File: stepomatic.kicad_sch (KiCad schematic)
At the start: 31 parts, among them J1 I2C, J2 28BYJ-48, J4 USB_B_Micro, Q1 MMBT3904, Q2 MMBT3904, SW1 Mode, SW2 RST, U1 HDC1080DMBR, U2 AMS1117-3.3, U3 ULN2003A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

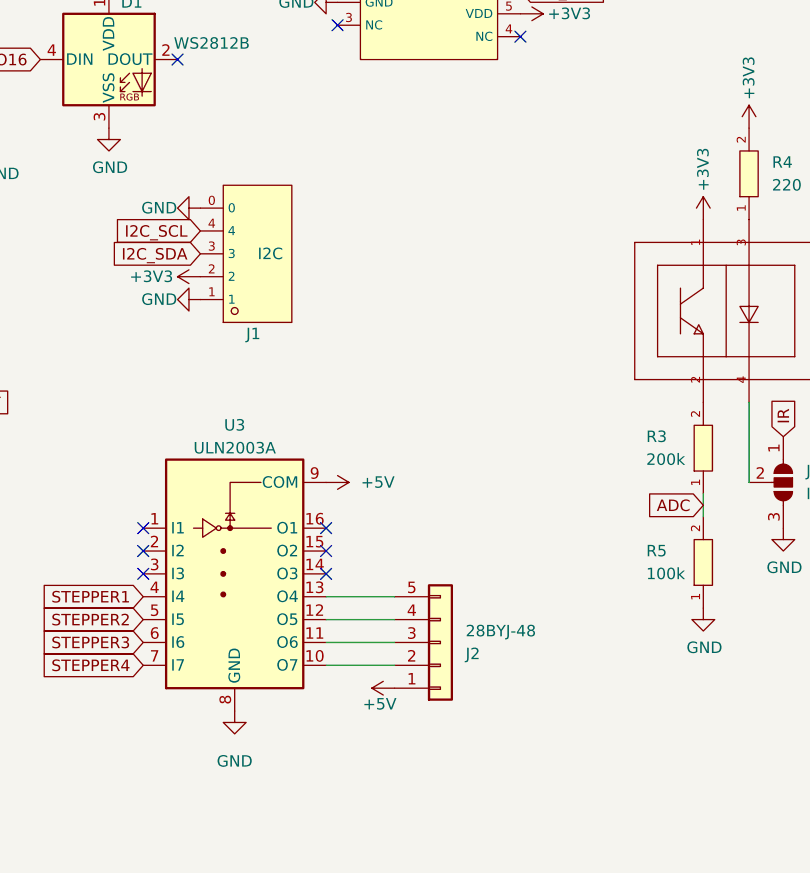
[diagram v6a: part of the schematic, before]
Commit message: Fix orientation of the stepper motor plug
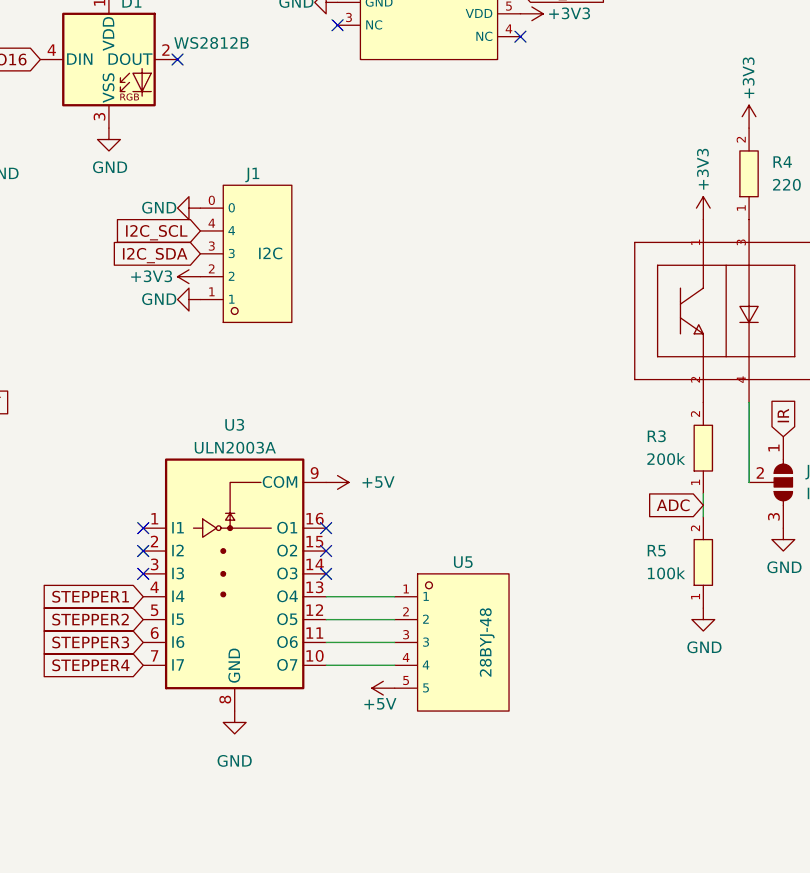
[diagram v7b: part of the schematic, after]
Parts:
- removed J2: 28BYJ-48, footprint:CONN-TH_B5B-XH-A-LF-SN, symbol Connector_Generic:Conn_01x05
- added U5: 28BYJ-48, footprint:CONN-TH_B5B-XH-A-LF-SN, symbol B5B-XH-A_(LF)(SN):B5B-XH-A_(LF)(SN)
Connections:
- net +5V: now also U5.5
- net at U3.10 (O7): now also U5.4
- net at U3.11 (O6): now also U5.3
- net at U3.12 (O5): now also U5.2
- net at U3.13 (O4): now also U5.1
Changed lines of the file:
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@@
   (symbol (lib_id "BM04B-SRSS-TB(LF)(SN):BM04B-SRSS-TB(LF)(SN)") (at 201.93 91.44 0) (mirror x) (unit 1)
     (in_bom yes) (on_board yes)
-    (property "Reference" "J1" (id 0) (at 201.93 100.33 0)
+    (property "Reference" "J1" (id 0) (at 201.93 82.55 0)
       (effects (font (size 1.27 1.27)) (justify left))
     )
@@
     )
     (pin "1")
+  )
+  (symbol (lib_id "B5B-XH-A_(LF)(SN):B5B-XH-A_(LF)(SN)") (at 224.79 134.62 0) (unit 1)
+    (in_bom yes) (on_board yes)
+    (property "Reference" "U5" (id 0) (at 226.06 125.73 0))
+    (property "Value" "28BYJ-48" (id 1) (at 228.6 134.62 90))
+    (property "Footprint" "footprint:CONN-TH_B5B-XH-A-LF-SN" (id 2) (at 224.79 144.78 0)
+      (effects (font (size 1.27 1.27) italic) hide)
+    )
+    (property "Datasheet" "https://atta.szlcsc.com/upload/public/pdf/source/20180319/EA947BC272645EB2E2B2116BA052A949.pdf" (id 3) (at 222.504 134.493 0)
+      (effects (font (size 1.27 1.27)) (justify left) hide)
+    )
+    (property "LCSC" "C157991" (id 4) (at 224.79 134.62 0)
+      (effects (font (size 1.27 1.27)) hide)
+    )
+    (pin "1")
+    (pin "2")
+    (pin "3")
+    (pin "4")
+    (pin "5")
   )
   (symbol (lib_id "power:+3V3") (at 186.69 62.23 0) (mirror y) (unit 1)
@@
     (pin "1")
   )
-  (symbol (lib_id "Connector_Generic:Conn_01x05") (at 223.52 134.62 0) (mirror x) (unit 1)
-    (in_bom yes) (on_board yes) (fields_autoplaced)
-    (property "Reference" "J2" (id 0) (at 226.314 135.8901 0)
-      (effects (font (size 1.27 1.27)) (justify left))
-    )
-    (property "Value" "28BYJ-48" (id 1) (at 226.314 133.3501 0)
-      (effects (font (size 1.27 1.27)) (justify left))
-    )
-    (property "Footprint" "footprint:CONN-TH_B5B-XH-A-LF-SN" (id 2) (at 223.52 134.62 0)
-      (effects (font (size 1.27 1.27)) hide)
-    )
-    (property "Datasheet" "~" (id 3) (at 223.52 134.62 0)
-      (effects (font (size 1.27 1.27)) hide)
-    )
-    (property "LCSC" "C157991" (id 6) (at 226.314 135.8901 0)
-      (effects (font (size 1.27 1.27)) hide)
-    )
-    (pin "1")
-    (pin "2")
-    (pin "3")
-    (pin "4")
-    (pin "5")
-  )
   (symbol (lib_id "power:GND") (at 62.23 104.14 0) (unit 1)
     (in_bom yes) (on_board yes)
@@
       (reference "J1") (unit 1) (value "I2C") (footprint "footprint:CONN-SMD_BM04B-SRSS-TB")
     )
-    (path "/daa4d8a1-8f94-4834-94ac-ea4f5a8e3b41"
-      (reference "J2") (unit 1) (value "28BYJ-48") (footprint "footprint:CONN-TH_B5B-XH-A-LF-SN")
-    )
     (path "/c93b24b6-f087-4eeb-a88b-a9a714a140bb"
       (reference "J4") (unit 1) (value "USB_B_Micro") (footprint "Connector_USB:USB_Micro-B_Molex-105017-0001")
@@
       (reference "U4") (unit 1) (value "CH340C") (footprint "Package_SO:SOIC-16_3.9x9.9mm_P1.27mm")
     )
+    (path "/1718d297-773a-44c9-b95f-932ebdecfaf2"
+      (reference "U5") (unit 1) (value "28BYJ-48") (footprint "footprint:CONN-TH_B5B-XH-A-LF-SN")
+    )
     (path "/ae7b485a-7198-4807-96a8-111bb9defe9c"

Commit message: Tidy up for review
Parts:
- C1, C4: value 100nF -> 100n
- C5, C7: value 10uF -> 10u
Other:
- note removed: "Add test points"
- note removed: "https://rayshobby.net/wordpress/tips-and-tricks-for-using-esp8266/"
- moved on the sheet: C1, C2, C3, C4, C5, C7, CGQ1, D1, H1, H2, H3, H4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
